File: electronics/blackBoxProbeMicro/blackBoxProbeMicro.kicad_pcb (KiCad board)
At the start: 4 copper layers, 29 x 29 mm, 67 parts, among them J1 USB-C, J2 JTAG_2X05, J3 JTAG_2X05, J4 DevBoardUartOutput, Q1 BSD840N, Q2 NTJD4152P, U1 MCP1702-MB, U2 DT1446-04S, U3 STM32F103CBT, Y1 8MHz

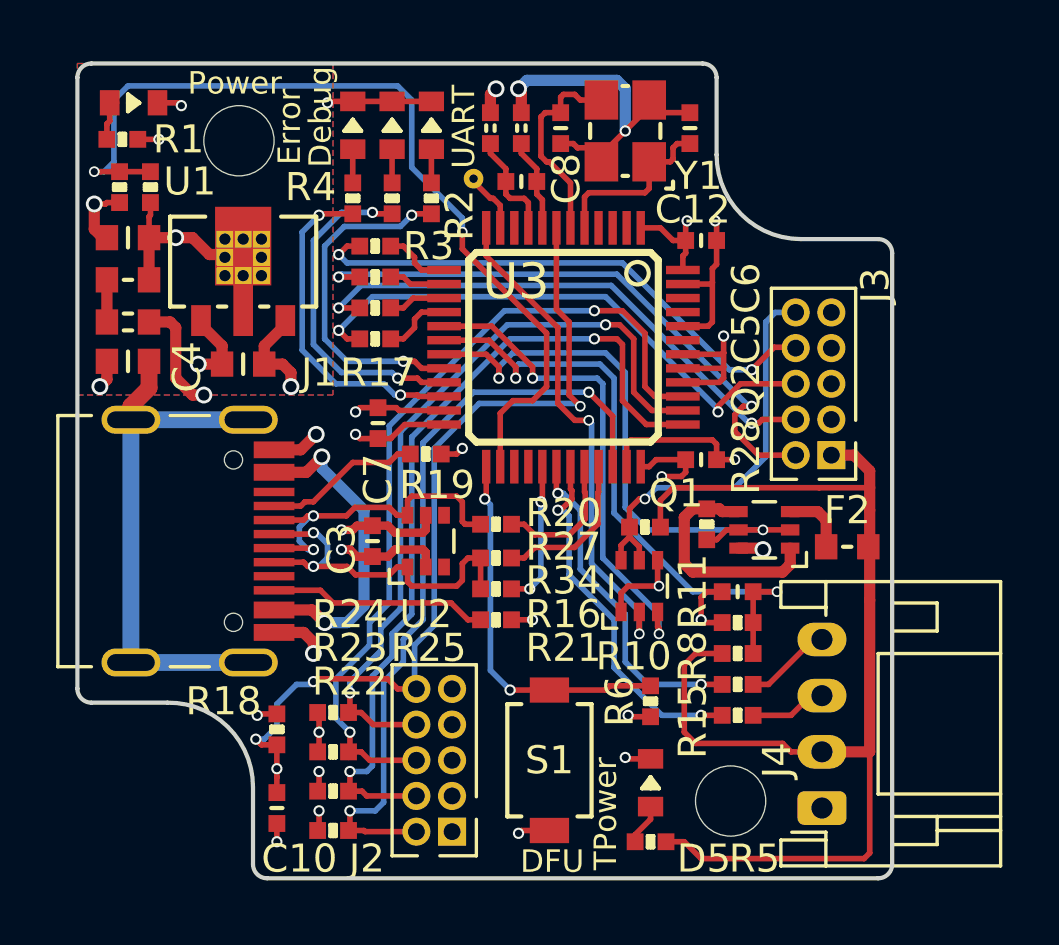
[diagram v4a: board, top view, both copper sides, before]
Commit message: fixing ERC/DRC errors after component updates
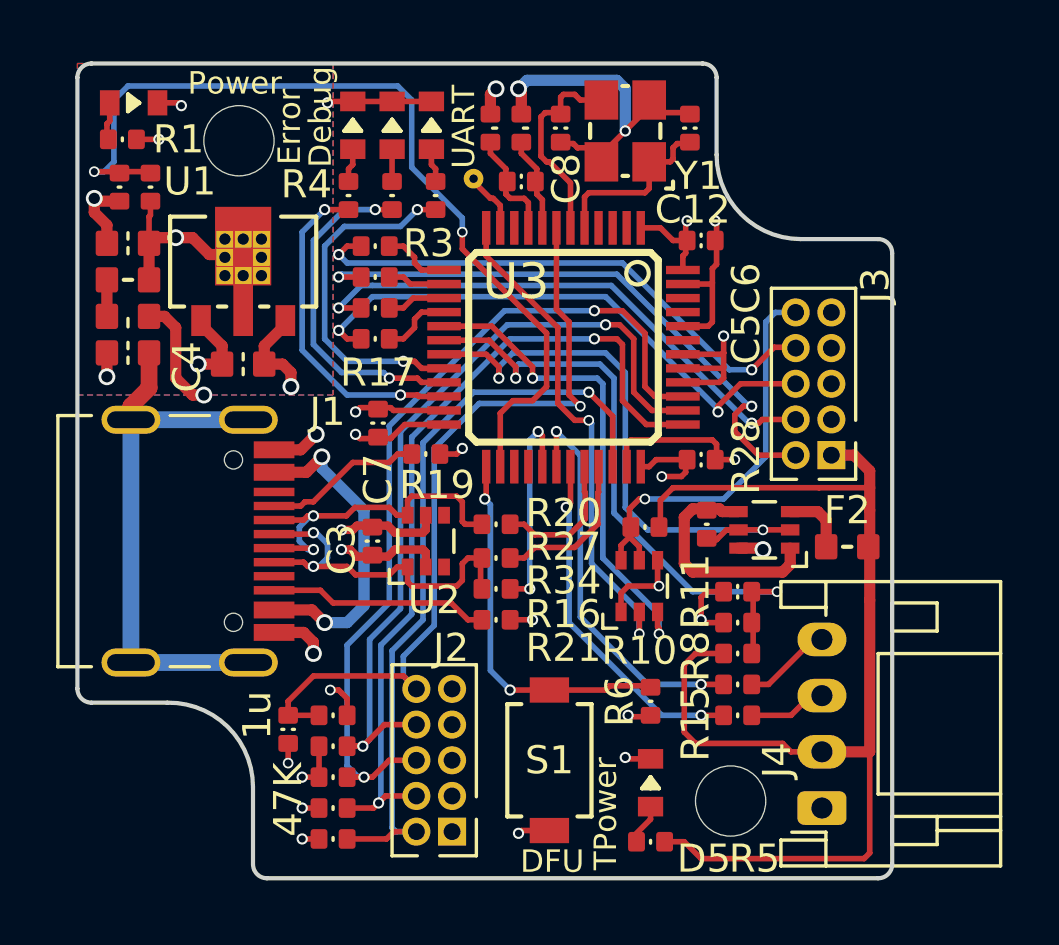
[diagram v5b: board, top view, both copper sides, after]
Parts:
- moved C10 2.83 mm to (140.5, 110.7)
- moved R18 2.06 mm to (142.1, 110.2), turned to 180 degrees
- moved R25 1.20 mm to (142.1, 111.3)
- moved R24 0.90 mm to (142.1, 112.4)
- moved R23 0.60 mm to (142.1, 113.5)
- moved C2 0.30 mm to (134.8, 97.3)
- moved R22 0.30 mm to (142.1, 114.6)
- moved C1 0.20 mm to (134.8, 93.4)
- moved FB1 0.20 mm to (134.8, 96.0)
- moved R2 0.18 mm to (145.8, 91.7)
- moved R4 0.18 mm to (142.7, 91.7)
- moved R3 0.10 mm to (144.2, 91.7)
- turned Q1 to 90 degrees
- turned Q2 to 180 degrees
- turned U2 to 90 degrees
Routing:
- net /MCU_RST: track 31.2 -> 28.5 mm, vias 4 -> 1
- net /USB_PU: track 5.19 -> 7.69 mm
- net /PROBE_I_TX: track 11.9 -> 14.2 mm
- net /MCU_TDI: track 27.4 -> 29.1 mm
- net /MCU_TDO: track 29.7 -> 31.3 mm
- net /VDD: track 25.5 -> 26.5 mm
- net /MCU_TMS: track 27.5 -> 27.3 mm, vias 2 -> 1

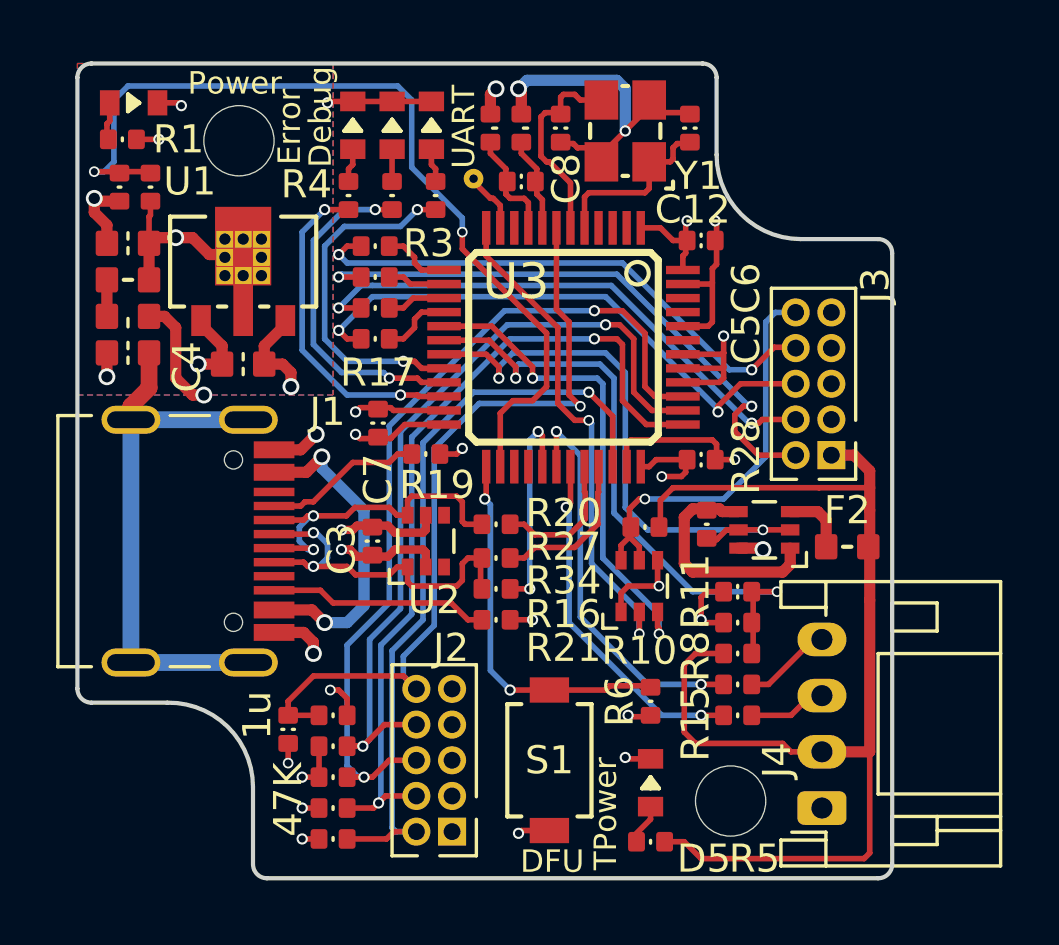
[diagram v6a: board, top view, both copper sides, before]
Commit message: added additional ground planes top and bottom
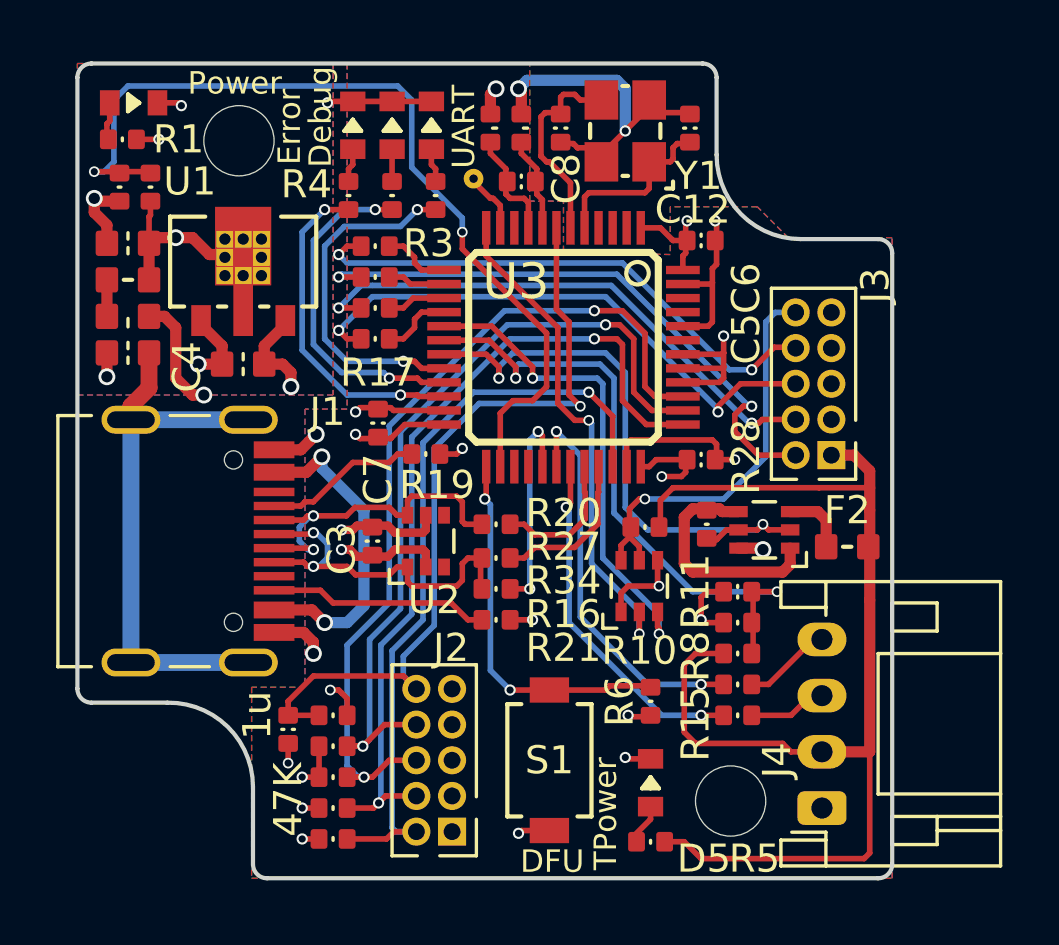
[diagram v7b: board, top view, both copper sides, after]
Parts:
- N2: value V:20230224 -> V:20230929
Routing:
- added copper zone on B.Cu, net /VSS
- added copper zone on F.Cu, net /VSS

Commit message: WIP adapting to aisler DRC
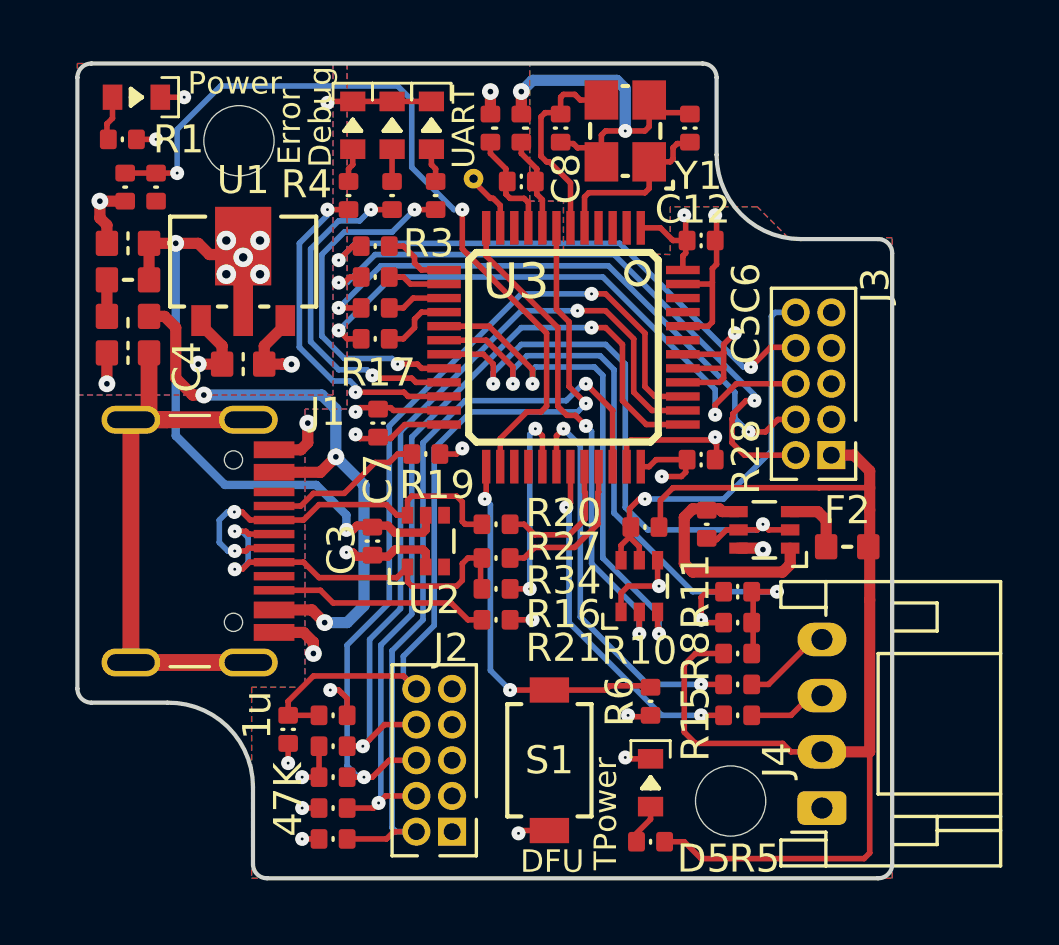
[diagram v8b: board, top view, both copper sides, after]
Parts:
- N2: value V:20230929 -> V:20231214
- U1: footprint SquantorIC:SOT89-NXP-Viatab -> SquantorIC:SOT89-NXP
- moved D1 0.22 mm to (135.1, 88.2)
- moved R7 0.20 mm to (135.8, 91.4)
- moved R12 0.20 mm to (134.7, 91.4)
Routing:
- net /USB_V: track 32.2 -> 28.8 mm
- net /VUSB: track 26.4 -> 23.9 mm, vias 2 -> 7
- net /USB_D_C-: track 12.3 -> 14.4 mm
- net /USB_D_C+: track 13.3 -> 15.3 mm
- net /PROBE_E_TMS: track 21.3 -> 22.8 mm
- net /PROBE_E_TCK: track 19.4 -> 20.8 mm
- net /PROBE_E_TDO: track 19.9 -> 21.1 mm
- net /PROBE_I_RST_SEN: track 17.3 -> 18.3 mm
- net /VSS: track 54.5 -> 55.4 mm
- net /VBUS: track 22.0 -> 21.1 mm
- net /TARGET_PWR_SENSE: track 22.3 -> 23.1 mm
- net /TARGET_PWR_EN: track 21.6 -> 22.4 mm
